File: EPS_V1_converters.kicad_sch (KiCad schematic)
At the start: 46 parts, among them U2 TPS62132RGTR, U3 TPS62133RGTR, U4 MP28167GQ-Z, U6 TPS61088RHLR

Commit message: Clarify global net naming, other minor fixes
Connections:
- net VOUT renamed CHG_OUT
- net VSOLAR renamed SOLAR
- net VSOLARR renamed SOLAR_5V
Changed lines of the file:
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@@
-	)
-	(junction
-		(at 186.69 68.58)
-		(diameter 0)
-		(color 0 0 0 0)
 	)
 	(junction
@@
 	)
 	(junction
-		(at 185.42 68.58)
-		(diameter 0)
-		(color 0 0 0 0)
-	)
-	(junction
 		(at 132.08 72.39)
 		(diameter 0)
@@
 	)
 	(junction
-		(at 189.23 68.58)
-		(diameter 0)
-		(color 0 0 0 0)
-	)
-	(junction
 		(at 114.3 49.53)
 		(diameter 0)
@@
 	(junction
 		(at 68.58 39.37)
-		(diameter 0)
-		(color 0 0 0 0)
-	)
-	(junction
-		(at 185.42 69.85)
 		(diameter 0)
 		(color 0 0 0 0)
@@
 	(wire
 		(pts
-			(xy 189.23 68.58) (xy 186.69 68.58)
-		)
-		(stroke
-			(width 0)
-			(type default)
-		)
-	)
-	(wire
-		(pts
 			(xy 114.3 59.69) (xy 113.03 59.69)
 		)
@@
 	(wire
 		(pts
-			(xy 186.69 68.58) (xy 186.69 69.85)
-		)
-		(stroke
-			(width 0)
-			(type default)
-		)
-	)
-	(wire
-		(pts
 			(xy 186.69 33.02) (xy 190.5 33.02)
 		)
@@
 	(wire
 		(pts
-			(xy 184.15 69.85) (xy 185.42 69.85)
-		)
-		(stroke
-			(width 0)
-			(type default)
-		)
-	)
-	(wire
-		(pts
 			(xy 190.5 35.56) (xy 189.23 35.56)
 		)
@@
 	(wire
 		(pts
-			(xy 185.42 68.58) (xy 185.42 69.85)
-		)
-		(stroke
-			(width 0)
-			(type default)
-		)
-	)
-	(wire
-		(pts
 			(xy 105.41 49.53) (xy 114.3 49.53)
 		)
@@
 	(wire
 		(pts
-			(xy 184.15 68.58) (xy 184.15 69.85)
-		)
-		(stroke
-			(width 0)
-			(type default)
-		)
-	)
-	(wire
-		(pts
 			(xy 105.41 46.99) (xy 114.3 46.99)
 		)
@@
 	(wire
 		(pts
-			(xy 185.42 68.58) (xy 184.15 68.58)
-		)
-		(stroke
-			(width 0)
-			(type default)
-		)
-	)
-	(wire
-		(pts
 			(xy 34.29 153.67) (xy 45.72 153.67)
 		)
@@
 	(wire
 		(pts
-			(xy 186.69 68.58) (xy 185.42 68.58)
-		)
-		(stroke
-			(width 0)
-			(type default)
-		)
-	)
-	(wire
-		(pts
 			(xy 186.69 43.18) (xy 190.5 43.18)
 		)
@@
 	(wire
 		(pts
-			(xy 185.42 69.85) (xy 186.69 69.85)
-		)
-		(stroke
-			(width 0)
-			(type default)
-		)
-	)
-	(wire
-		(pts
 			(xy 168.91 30.48) (xy 179.07 30.48)
 		)
@@
 		)
 	)
-	(global_label "VSOLAR"
+	(global_label "SOLAR"
 		(shape passive)
 		(at 156.21 30.48 180)
@@
 		)
 		(property "Intersheetrefs" "${INTERSHEET_REFS}"
-			(at 147.3208 30.48 0)
+			(at 148.4094 30.48 0)
 			(effects
 				(font
@@
 		)
 	)
-	(global_label "VSOLARR"
+	(global_label "SOLAR_5V"
 		(shape passive)
 		(at 271.78 40.64 0)
@@
 		)
 		(property "Intersheetrefs" "${INTERSHEET_REFS}"
-			(at 281.9392 40.64 0)
+			(at 282.8463 40.64 0)
 			(effects
 				(font
@@
 		)
 	)
-	(global_label "VOUT"
+	(global_label "CHG_OUT"
 		(shape passive)
 		(at 31.75 114.3 180)
@@
 		)
 		(property "Intersheetrefs" "${INTERSHEET_REFS}"
-			(at 25.1589 114.3 0)
+			(at 21.4094 114.3 0)
 			(effects
 				(font
@@
 		(on_board yes)
 		(dnp no)
-		(fields_autoplaced yes)
 		(property "Reference" "#PWR016"
 			(at 143.51 175.26 0)
@@
 		)
 		(property "Value" "+3V3"
-			(at 143.51 166.37 0)
-			(effects
-				(font
+			(at 143.51 167.386 0)
+			(effects
+				(font

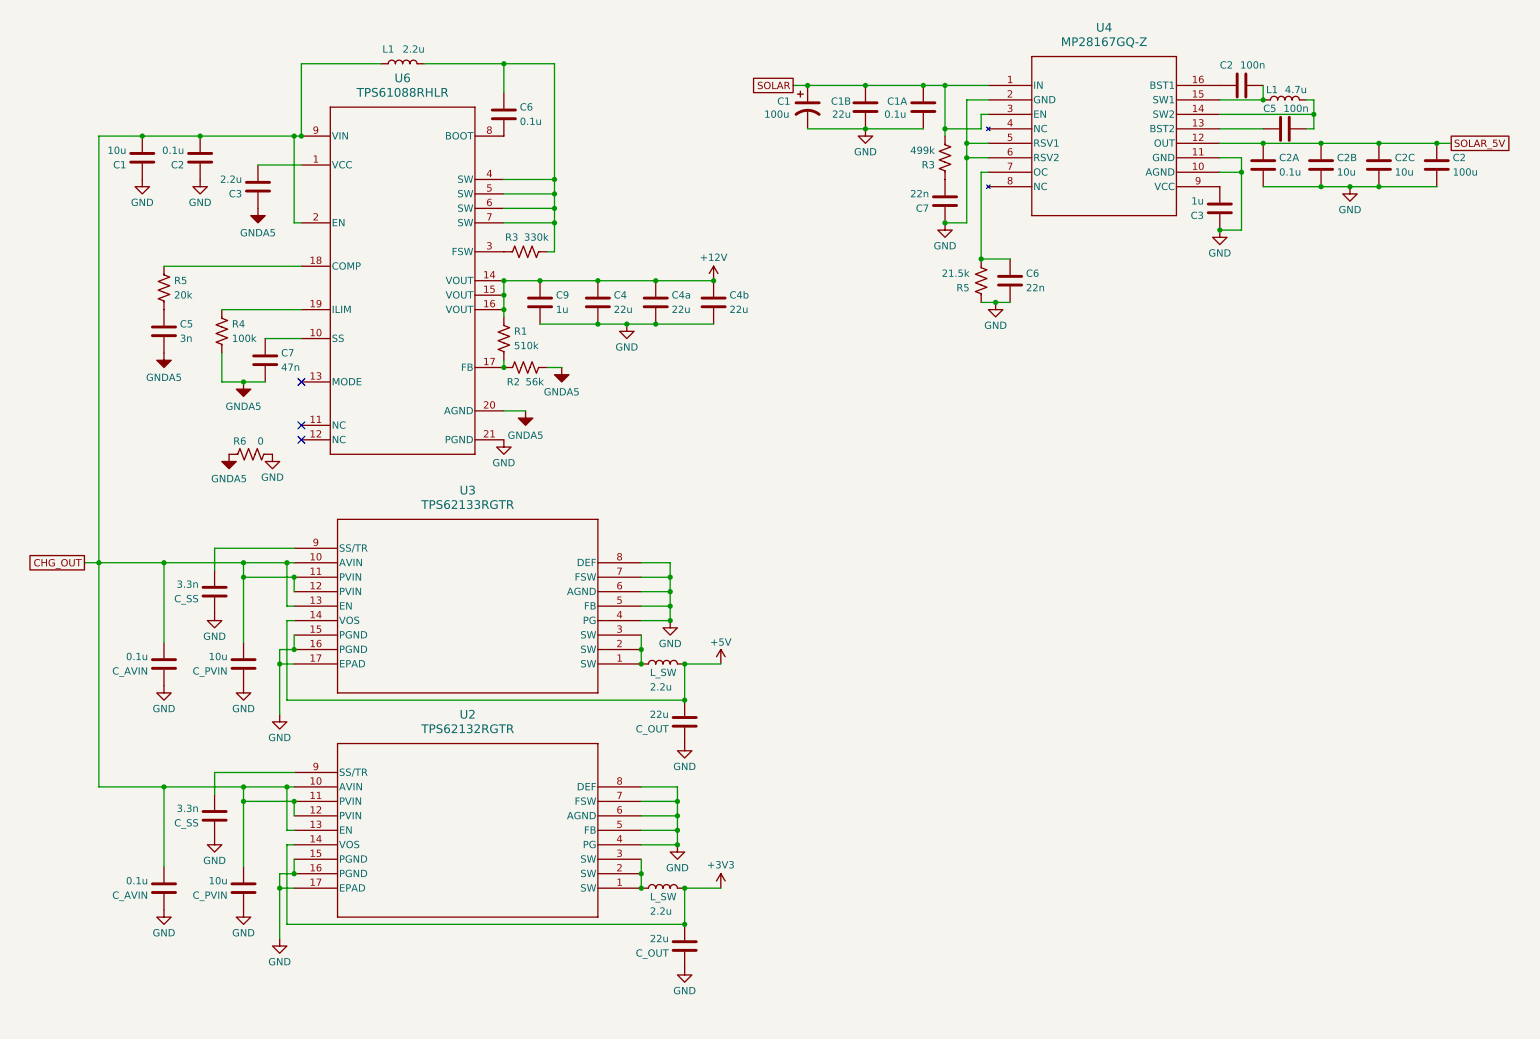
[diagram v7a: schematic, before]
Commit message: Add all footprints except connectors & switches, change to net ties over 0 ohm resistors
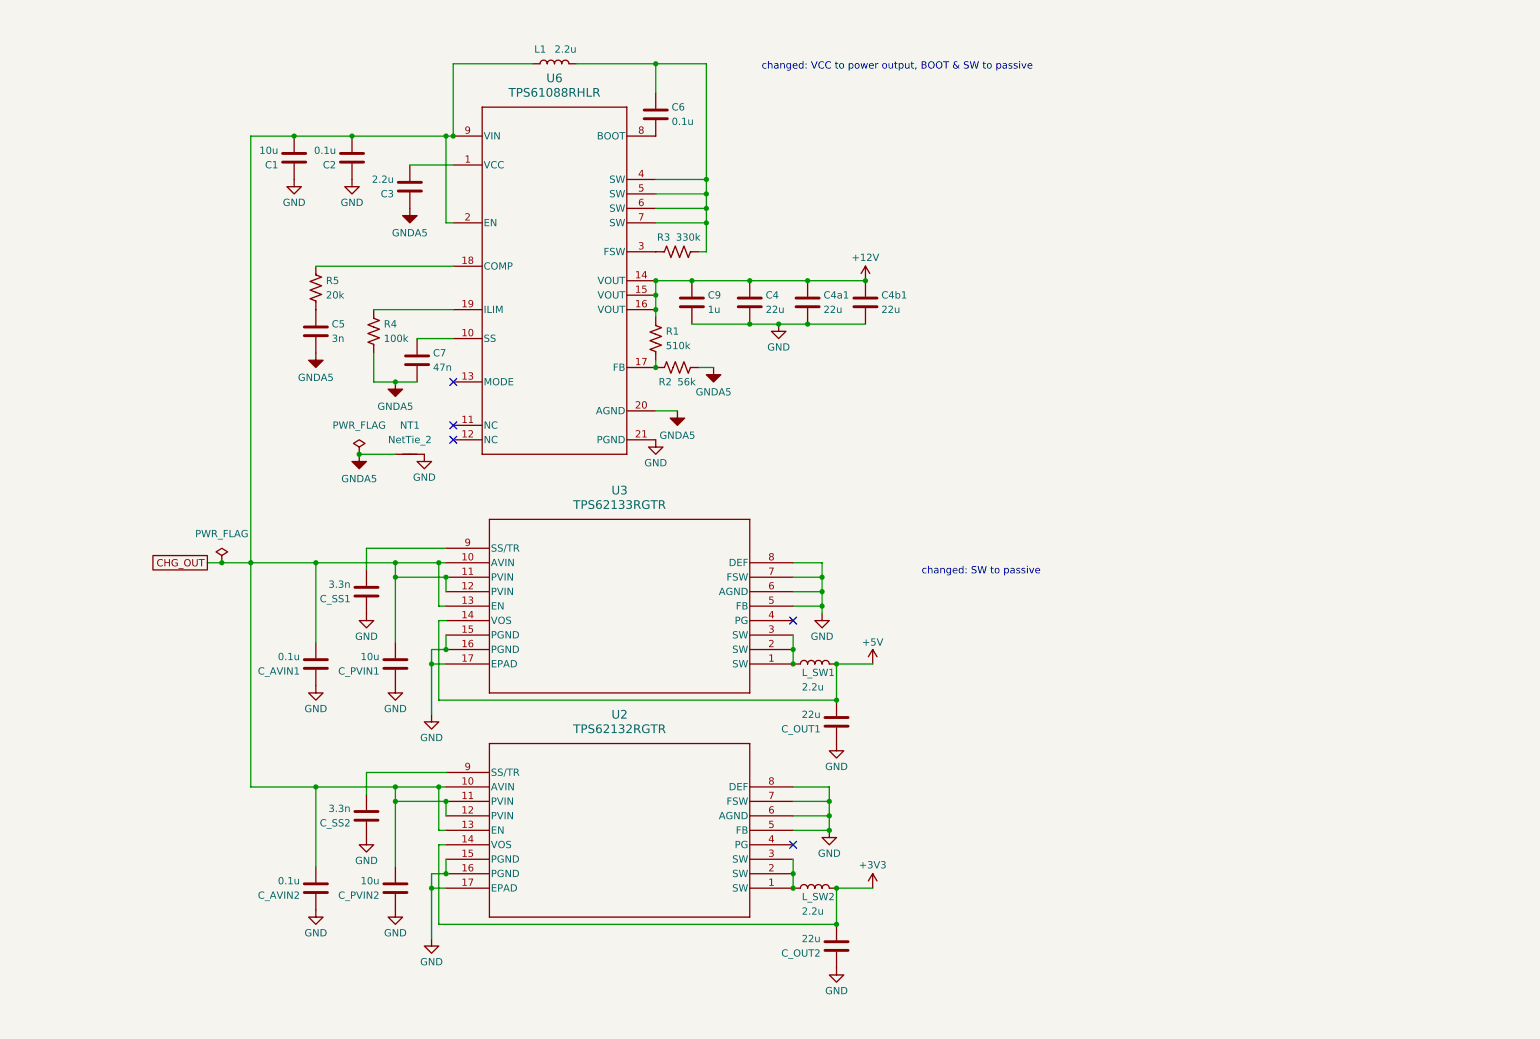
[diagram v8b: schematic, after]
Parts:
- removed C1: 100u, symbol Device:C_Polarized_US
- removed C1A, C2A: 0.1u, symbol Device:C
- removed C1B: 22u, symbol Device:C
- removed C2, C5: 100n, symbol Device:C
- removed C2: 100u, symbol Device:C
- removed C2B, C2C: 10u, symbol Device:C
- removed C3: 1u, symbol Device:C
- removed C6, C7: 22n, symbol Device:C
- removed L1: 4.7u, symbol Device:L
- removed R3: 499k, symbol Device:R_US
- removed R5: 21.5k, symbol Device:R_US
- removed R6: 0, symbol Device:R_US
- removed U4: MP28167GQ-Z, MP28167GQ-Z:QFN-16_MP28167GQ_MNP, symbol MP28167GQ-Z:MP28167GQ-Z
- added NT1: NetTie_2, NetTie:NetTie-2_SMD_Pad2.0mm, symbol Device:NetTie_2
- C1: footprint (none) -> Capacitor_SMD:C_0805_2012Metric; Voltage Rating (none) -> 25V
- C2, C3, C6: footprint (none) -> Capacitor_SMD:C_0603_1608Metric; Voltage Rating (none) -> 16V
- C4: footprint (none) -> Capacitor_SMD:C_1206_3216Metric; Voltage Rating (none) -> 35V
- C4a1: renamed from C4a; footprint (none) -> Capacitor_SMD:C_1206_3216Metric; Voltage Rating (none) -> 35V
- C4b1: renamed from C4b; footprint (none) -> Capacitor_SMD:C_1206_3216Metric; Voltage Rating (none) -> 35V
- C5, C7: footprint (none) -> Capacitor_SMD:C_0603_1608Metric; Voltage Rating (none) -> 10V
- C9: footprint (none) -> Capacitor_SMD:C_0603_1608Metric; Voltage Rating (none) -> 25V
- C_AVIN1, C_AVIN2: renamed from C_AVIN; footprint (none) -> Capacitor_SMD:C_0603_1608Metric; Voltage Rating (none) -> 16V
- C_OUT1: renamed from C_OUT; footprint (none) -> Capacitor_SMD:C_0805_2012Metric; Voltage Rating (none) -> 25V
- C_OUT2: renamed from C_OUT; footprint (none) -> Capacitor_SMD:C_0805_2012Metric; Voltage Rating (none) -> 16V
- C_PVIN1, C_PVIN2: renamed from C_PVIN; footprint (none) -> Capacitor_SMD:C_0805_2012Metric; Voltage Rating (none) -> 25V
- C_SS1, C_SS2: renamed from C_SS; footprint (none) -> Capacitor_SMD:C_0603_1608Metric; Voltage Rating (none) -> 16V
- L1: footprint (none) -> IFSC1515AHER2R2M01:IND_IFSC_1515AH_VIS; MPN (none) -> IFSC1515AHER2R2M01
- L_SW1, L_SW2: renamed from L_SW; footprint (none) -> IFSC1515AHER2R2M01:IND_IFSC_1515AH_VIS; MPN (none) -> IFSC1515AHER2R2M01
- R1, R2, R3, R4, R5: footprint (none) -> Resistor_SMD:R_0603_1608Metric
- U6: footprint RHL0020A -> TPS61088RHLR:RHL0020A
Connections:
- net GND: now also NT1.2; no longer U2.4 (PG), U3.4 (PG)
- net GNDA5: now also NT1.1
- no-connect marks 3 -> 5
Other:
- note added: "changed: SW to passive"
- note added: "changed: VCC to power output, BOOT & SW to passive"
- moved on the sheet: C1, C2, C3, C4, C4a1, C4b1, C5, C6, C7, C9, C_AVIN1, C_AVIN2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
